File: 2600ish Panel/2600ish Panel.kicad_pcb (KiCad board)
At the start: 2 copper layers, 50.5 x 128.5 mm, 0 parts

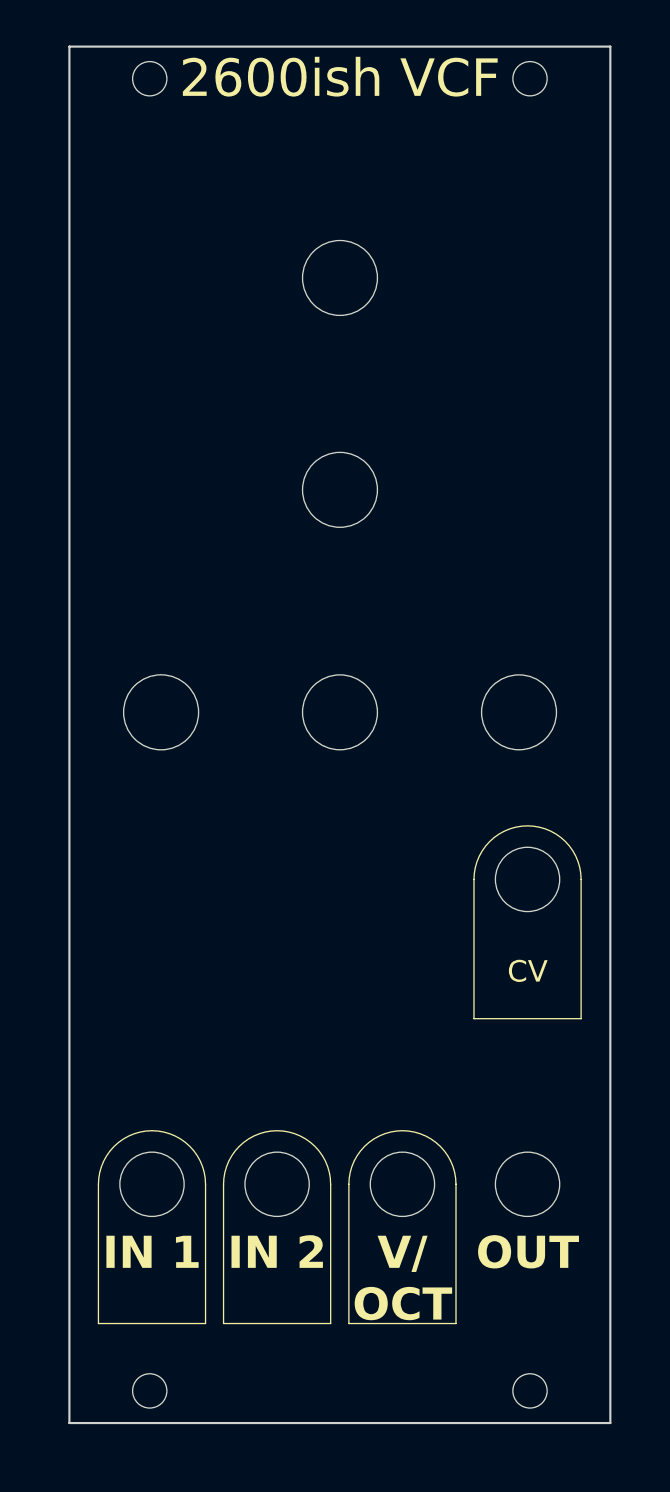
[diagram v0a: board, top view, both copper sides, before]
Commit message: New panel design with topography
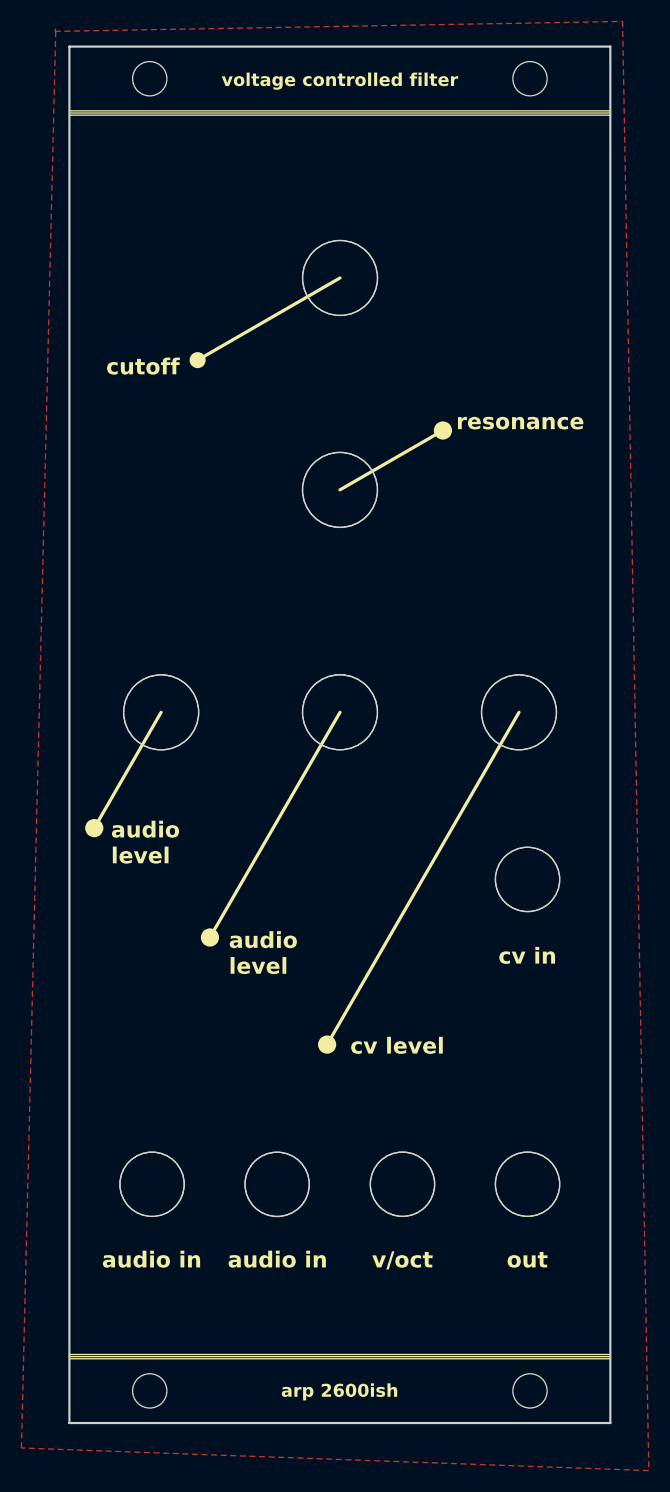
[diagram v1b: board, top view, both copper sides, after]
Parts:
- added G***: LOGO, LOGO, F.Cu at (184.2, 88.6)
- added REF**: MountingHole_6mm, MountingHole:MountingHole_6mm, F.Cu at (166.6, 130.7)
- added REF**: MountingHole_6mm, MountingHole:MountingHole_6mm, F.Cu at (201.7, 102.2)
- added REF**: MountingHole_6mm, MountingHole:MountingHole_6mm, F.Cu at (178.3, 130.7)
- added REF**: MountingHole_7mm, MountingHole:MountingHole_7mm, F.Cu at (184.2, 86.6)
- added REF**: MountingHole_6mm, MountingHole:MountingHole_6mm, F.Cu at (190.0, 130.7)
- added REF**: MountingHole_7mm, MountingHole:MountingHole_7mm, F.Cu at (184.2, 46.1)
- added REF**: MountingHole_7mm, MountingHole:MountingHole_7mm, F.Cu at (184.2, 65.9)
- added REF**: MountingHole_7mm, MountingHole:MountingHole_7mm, F.Cu at (200.9, 86.7)
- added REF**: MountingHole_7mm, MountingHole:MountingHole_7mm, F.Cu at (167.5, 86.7)
- added REF**: MountingHole_6mm, MountingHole:MountingHole_6mm, F.Cu at (201.7, 130.7)
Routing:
- added copper zone on F.Cu, net (none)
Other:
- board text added: "WayWayWay"
- board text added: "arp 2600ish"
- board text added: "audio in"
- board text added: "audio level"
- board text added: "cutoff"
- board text added: "cv in"
- board text added: "cv level"
- board text added: "out"
- board text added: "resonance"
- board text added: "v/oct"
- board text added: "voltage controlled filter"
- board text removed: "2600ish VCF"
- board text removed: "CV"
- board text removed: "IN 1"
- board text removed: "IN 2"
- board text removed: "OUT"
- board text removed: "V/ OCT"
